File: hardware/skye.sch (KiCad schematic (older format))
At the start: 11 parts, among them IC1 ATTINY85-20SUR, P1 IO, P2 IO, P3 USB_A, U1 WS2812

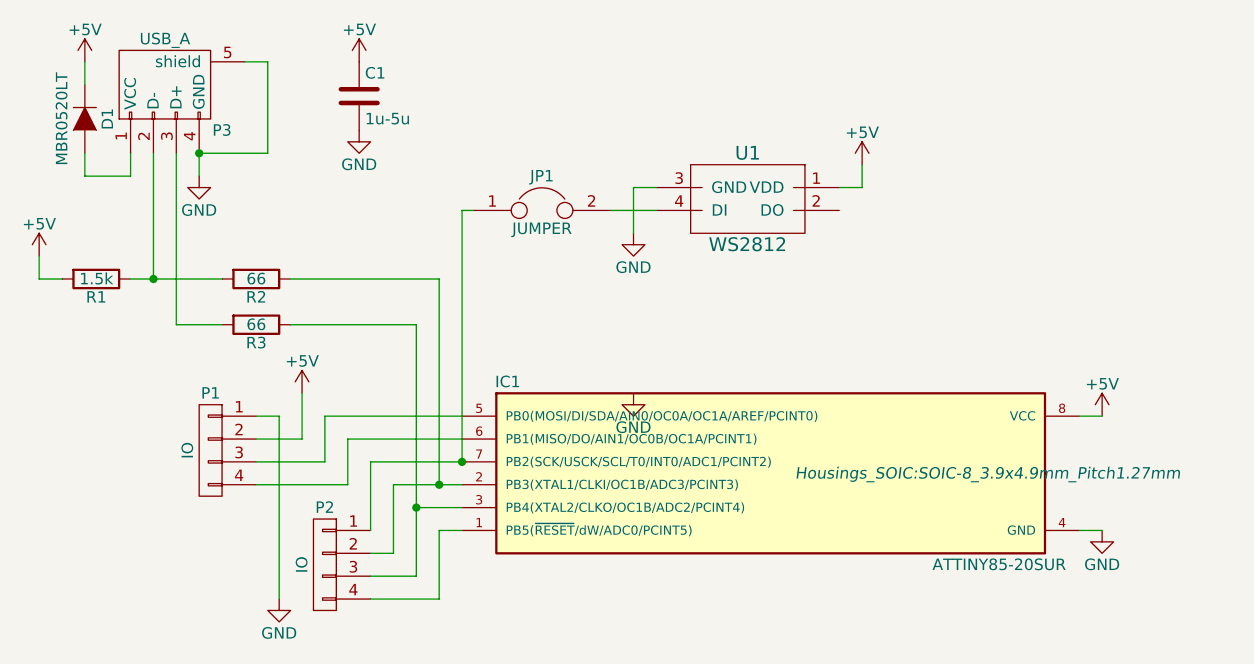
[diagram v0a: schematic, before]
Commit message: Added zenier diodes
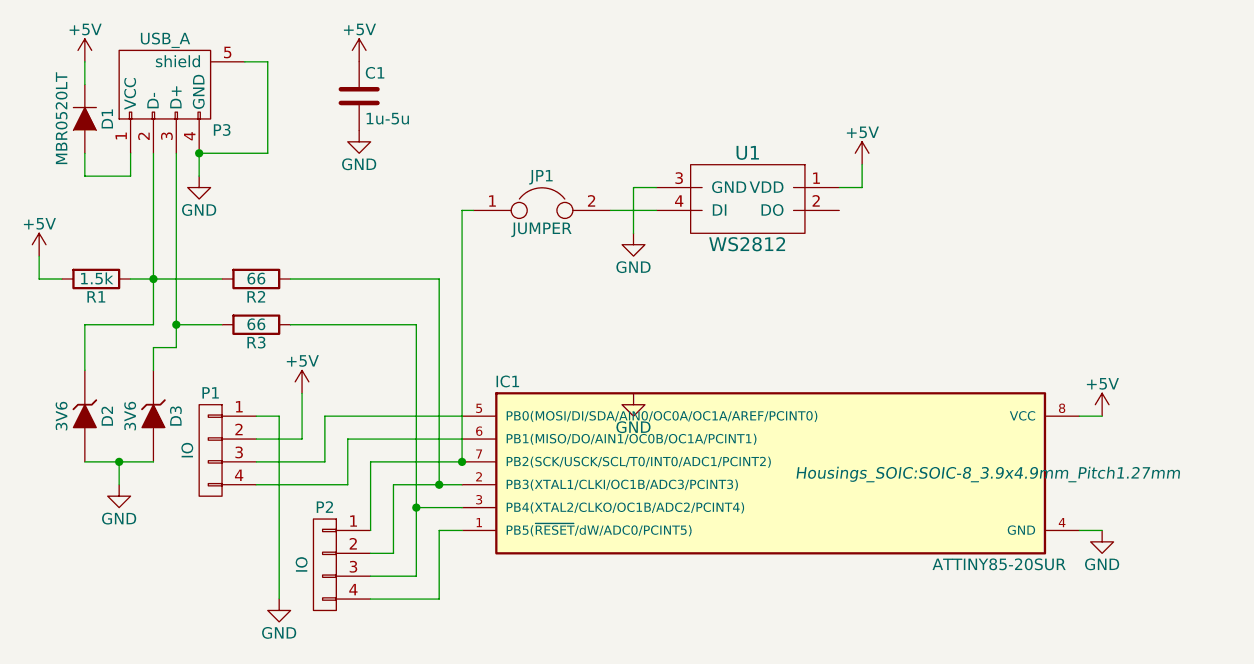
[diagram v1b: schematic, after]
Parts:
- added D2, D3: 3V6, Diodes_SMD:SOD-323, symbol ZENER
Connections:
- net GND: now also D2.2 (A), D3.2 (A)
- net at P3.2 (D-), R1.1, R2.2: now also D2.1 (K)
- net at P3.3 (D+), R3.2: now also D3.1 (K)
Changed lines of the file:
@@
 	1    0    0    -1
 $EndComp
-Wire Wire Line
-	3400 2650 3400 2750
-Wire Wire Line
-	3300 2650 3300 3400
-Wire Wire Line
-	3300 3400 3500 3400
-Wire Wire Line
-	3200 2650 3200 3200
-Wire Wire Line
-	3100 3200 3500 3200
-Wire Wire Line
-	2900 2250 2900 2350
-Wire Wire Line
-	3100 2650 3100 2750
-Wire Wire Line
-	3100 2750 2900 2750
-Wire Wire Line
-	2900 2750 2900 2650
-Wire Wire Line
-	7250 3800 7350 3800
-Wire Wire Line
-	7350 4300 7250 4300
-Wire Wire Line
-	3650 3800 3750 3800
-Wire Wire Line
-	3650 3900 3850 3900
-Wire Wire Line
-	3850 3900 3850 3700
-Wire Wire Line
-	3650 4000 3950 4000
-Wire Wire Line
-	3950 4000 3950 3800
-Wire Wire Line
-	3950 3800 4550 3800
-Wire Wire Line
-	3650 4100 4050 4100
-Wire Wire Line
-	4050 4100 4050 3900
-Wire Wire Line
-	4050 3900 4550 3900
-Wire Wire Line
-	4550 4100 4250 4100
-Wire Wire Line
-	4250 4100 4250 4400
-Wire Wire Line
-	4550 4200 4350 4200
-Wire Wire Line
-	4350 3400 4350 4500
-Wire Wire Line
-	3800 3200 4450 3200
-Wire Wire Line
-	4450 3200 4450 4100
-Connection ~ 4450 4100
-Wire Wire Line
-	3800 3400 4350 3400
-Connection ~ 4350 4200
-Connection ~ 3200 3200
-Wire Wire Line
-	2700 3100 2700 3200
-Wire Wire Line
-	2700 3200 2800 3200
-Wire Wire Line
-	3750 3800 3750 4600
-Wire Wire Line
-	3600 2250 3700 2250
-Wire Wire Line
-	3700 2250 3700 2650
-Wire Wire Line
-	3700 2650 3400 2650
-Connection ~ 3400 2650
 $Comp
 L +5V #PWR09
@@
 	1    0    0    -1
 $EndComp
-Wire Wire Line
-	4550 4300 4450 4300
-Wire Wire Line
-	4450 4300 4450 4600
 $Comp
 L CONN_01X04 P1
@@
 	-1   0    0    -1
 $EndComp
-Wire Wire Line
-	4150 4000 4150 4300
-Wire Wire Line
-	4150 4000 4550 4000
-Wire Wire Line
-	4250 4400 4150 4400
-Wire Wire Line
-	4350 4500 4150 4500
-Wire Wire Line
-	4450 4600 4150 4600
 $Comp
 L WS2812 U1
@@
 	1    0    0    -1
 $EndComp
+$Comp
+L ZENER D2
+U 1 1 57723ECC
+P 2900 3800
+F 0 "D2" H 2900 3900 50  0000 C CNN
+F 1 "3V6" H 2900 3700 50  0000 C CNN
+F 2 "Diodes_SMD:SOD-323" H 2900 3800 50  0001 C CNN
+F 3 "" H 2900 3800 50  0000 C CNN
+	1    2900 3800
+	0    1    1    0
+$EndComp
+Wire Wire Line
+	3400 2650 3400 2750
+Wire Wire Line
+	3100 3200 3500 3200
+Wire Wire Line
+	2900 2250 2900 2350
+Wire Wire Line
+	3100 2650 3100 2750
+Wire Wire Line
+	3100 2750 2900 2750
+Wire Wire Line
+	2900 2750 2900 2650
+Wire Wire Line
+	7250 3800 7350 3800
+Wire Wire Line
+	7350 4300 7250 4300
+Wire Wire Line
+	3650 3800 3750 3800
+Wire Wire Line
+	3650 3900 3850 3900
+Wire Wire Line
+	3850 3900 3850 3700
+Wire Wire Line
+	3650 4000 3950 4000
+Wire Wire Line
+	3950 4000 3950 3800
+Wire Wire Line
+	3950 3800 4550 3800
+Wire Wire Line
+	3650 4100 4050 4100
+Wire Wire Line
+	4050 4100 4050 3900
+Wire Wire Line
+	4050 3900 4550 3900
+Wire Wire Line
+	4250 4100 4550 4100
+Wire Wire Line
+	4250 4100 4250 4400
+Wire Wire Line
+	4550 4200 4350 4200
+Wire Wire Line
+	4350 3400 4350 4500
+Wire Wire Line
+	3800 3200 4450 3200
+Wire Wire Line
+	4450 3200 4450 4100
+Connection ~ 4450 4100
+Wire Wire Line
+	3800 3400 4350 3400
+Connection ~ 4350 4200
+Connection ~ 3200 3200
+Wire Wire Line
+	2700 3100 2700 3200
+Wire Wire Line
+	2700 3200 2800 3200
+Wire Wire Line
+	3750 3800 3750 4600
+Wire Wire Line
+	3600 2250 3700 2250
+Wire Wire Line
+	3700 2250 3700 2650
+Wire Wire Line
+	3700 2650 3400 2650
+Connection ~ 3400 2650
+Wire Wire Line
+	4550 4300 4450 4300
+Wire Wire Line
+	4450 4300 4450 4600
+Wire Wire Line
+	4150 4000 4150 4300
+Wire Wire Line
+	4150 4000 4550 4000
+Wire Wire Line
+	4250 4400 4150 4400
+Wire Wire Line
+	4350 4500 4150 4500
+Wire Wire Line
+	4450 4600 4150 4600
 Wire Wire Line
 	5400 2800 5300 2800
@@
 	4550 2900 4550 4000
 Connection ~ 4550 4000
+Connection ~ 3300 3400
+Wire Wire Line
+	3300 3400 3500 3400
+$Comp
+L ZENER D3
+U 1 1 57723E13
+P 3200 3800
+F 0 "D3" H 3200 3900 50  0000 C CNN
+F 1 "3V6" H 3200 3700 50  0000 C CNN
+F 2 "Diodes_SMD:SOD-323" H 3200 3800 50  0001 C CNN
+F 3 "" H 3200 3800 50  0000 C CNN
+	1    3200 3800
+	0    1    1    0
+$EndComp
+Wire Wire Line
+	3200 2650 3200 3400
+Wire Wire Line
+	3300 2650 3300 3500
+Wire Wire Line
+	3300 3500 3200 3500
+Wire Wire Line
+	3200 3500 3200 3600
+Wire Wire Line
+	3200 3400 2900 3400
+Wire Wire Line
+	2900 3400 2900 3600
+Wire Wire Line
+	3200 4000 2900 4000
+Wire Wire Line
+	3050 4000 3050 4100
+Connection ~ 3050 4000
+$Comp
+L GND #PWR013
+U 1 1 57724AF7
+P 3050 4100
+F 0 "#PWR013" H 3050 3850 50  0001 C CNN
+F 1 "GND" H 3050 3950 50  0000 C CNN
+F 2 "" H 3050 4100 50  0000 C CNN
+F 3 "" H 3050 4100 50  0000 C CNN
+	1    3050 4100
+	1    0    0    -1
+$EndComp
 $EndSCHEMATC
